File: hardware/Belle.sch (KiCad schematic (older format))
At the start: 18 parts, among them P1 Bell CONN, P2 Battery CONN, P3 Flashing CONN, U1 74AHC1G14, U2 ESP-12, U3 AP2112

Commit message: interchange bell connectors #6
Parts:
- R2: value 51k -> 47k
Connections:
- net +3V3: now also P1.1 (P1); no longer R1.1
- net GND: now also R1.1; no longer P1.1 (P1)
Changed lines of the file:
@@
 P 2800 3500
 F 0 "R2" V 2900 3450 50  0000 L CNN
-F 1 "51k" V 2700 3450 50  0000 L CNN
+F 1 "47k" V 2700 3450 50  0000 L CNN
 F 2 "Resistors_SMD:R_1206_HandSoldering" H 2800 3500 50  0001 C CNN
 F 3 "" H 2800 3500 50  0000 C CNN
@@
 L +3.3V #PWR07
 U 1 1 58BBD349
-P 2400 3100
-F 0 "#PWR07" H 2400 2950 50  0001 C CNN
-F 1 "+3.3V" H 2400 3240 50  0000 C CNN
-F 2 "" H 2400 3100 50  0000 C CNN
-F 3 "" H 2400 3100 50  0000 C CNN
-	1    2400 3100
+P 2550 3900
+F 0 "#PWR07" H 2550 3750 50  0001 C CNN
+F 1 "+3.3V" H 2550 4040 50  0000 C CNN
+F 2 "" H 2550 3900 50  0000 C CNN
+F 3 "" H 2550 3900 50  0000 C CNN
+	1    2550 3900
 	1    0    0    -1
 $EndComp
@@
 L GND #PWR08
 U 1 1 58BBD44E
-P 2400 3750
-F 0 "#PWR08" H 2400 3500 50  0001 C CNN
-F 1 "GND" H 2400 3600 50  0000 C CNN
-F 2 "" H 2400 3750 50  0000 C CNN
-F 3 "" H 2400 3750 50  0000 C CNN
-	1    2400 3750
+P 2600 3050
+F 0 "#PWR08" H 2600 2800 50  0001 C CNN
+F 1 "GND" H 2600 2900 50  0000 C CNN
+F 2 "" H 2600 3050 50  0000 C CNN
+F 3 "" H 2600 3050 50  0000 C CNN
+	1    2600 3050
 	1    0    0    -1
 $EndComp
@@
 	2350 3500 2700 3500
 Wire Wire Line
-	2400 3600 2400 3750
-Wire Wire Line
 	4800 3700 5000 3700
 Wire Wire Line
@@
 Wire Wire Line
 	2400 3600 2350 3600
-Wire Wire Line
-	2400 3400 2400 3500
 Connection ~ 2400 3500
 Wire Wire Line
-	2400 3100 2400 3200
+	2400 3200 2400 3050
+Wire Wire Line
+	2400 3050 2600 3050
+Wire Wire Line
+	2400 3500 2400 3400
+Wire Wire Line
+	2400 3600 2400 3900
+Wire Wire Line
+	2400 3900 2550 3900
 $EndSCHEMATC

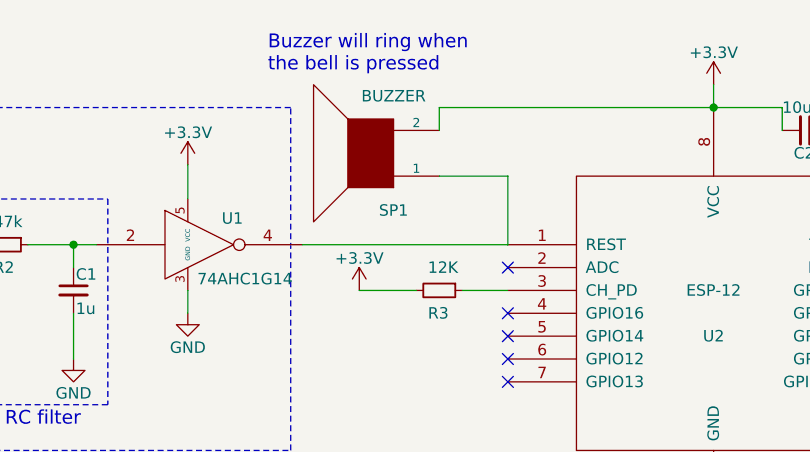
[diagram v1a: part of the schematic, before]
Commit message: add 10k resistor between RESET and Smidth Trigger output
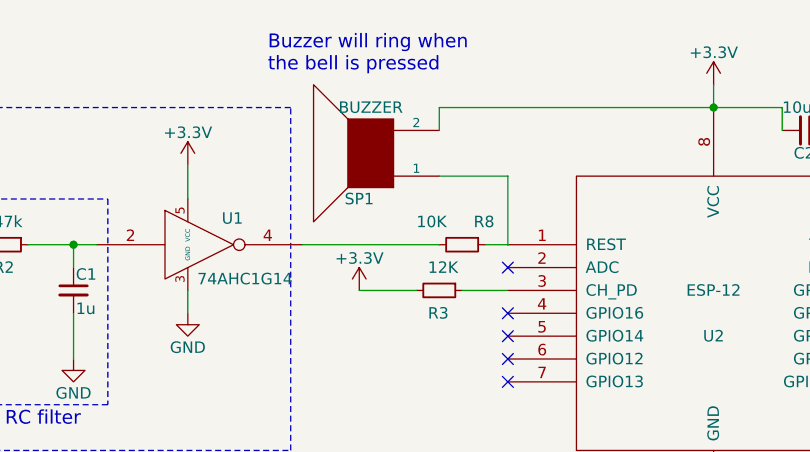
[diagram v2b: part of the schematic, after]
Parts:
- added R8: 10K, symbol R_Small
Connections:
- net at SP1.1, U2.1 (REST): now also R8.1; no longer U1.4
- new net: R8.2, U1.4
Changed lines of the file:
@@
 $EndComp
 $Comp
-L GND #PWR01
+L GND #PWR8
 U 1 1 58BBCCFC
 P 5900 4700
-F 0 "#PWR01" H 5900 4450 50  0001 C CNN
+F 0 "#PWR8" H 5900 4450 50  0001 C CNN
 F 1 "GND" H 5900 4550 50  0000 C CNN
 F 2 "" H 5900 4700 50  0000 C CNN
@@
 $EndComp
 $Comp
-L +3.3V #PWR02
+L +3.3V #PWR7
 U 1 1 58BBCD12
 P 5900 2800
-F 0 "#PWR02" H 5900 2650 50  0001 C CNN
+F 0 "#PWR7" H 5900 2650 50  0001 C CNN
 F 1 "+3.3V" H 5900 2940 50  0000 C CNN
 F 2 "" H 5900 2800 50  0000 C CNN
@@
 $EndComp
 $Comp
-L GND #PWR03
+L GND #PWR9
 U 1 1 58BBCDC5
 P 6650 3000
-F 0 "#PWR03" H 6650 2750 50  0001 C CNN
+F 0 "#PWR9" H 6650 2750 50  0001 C CNN
 F 1 "GND" H 6650 2850 50  0000 C CNN
 F 2 "" H 6650 3000 50  0000 C CNN
@@
 U 1 1 58BBCE20
 P 4400 3100
-F 0 "SP1" H 4300 3350 50  0000 C CNN
-F 1 "BUZZER" H 4300 2850 50  0000 C CNN
+F 0 "SP1" H 4450 3300 50  0000 C CNN
+F 1 "BUZZER" H 4400 2900 50  0000 C CNN
 F 2 "Belle:prosignal_buzzer" H 4400 3100 50  0001 C CNN
 F 3 "" H 4400 3100 50  0000 C CNN
@@
 $EndComp
 $Comp
-L GND #PWR04
+L GND #PWR5
 U 1 1 58BBD0DA
 P 3600 3800
-F 0 "#PWR04" H 3600 3550 50  0001 C CNN
+F 0 "#PWR5" H 3600 3550 50  0001 C CNN
 F 1 "GND" H 3600 3650 50  0000 C CNN
 F 2 "" H 3600 3800 50  0000 C CNN
@@
 $EndComp
 $Comp
-L +3.3V #PWR05
+L +3.3V #PWR4
 U 1 1 58BBD0F6
 P 3600 3150
-F 0 "#PWR05" H 3600 3000 50  0001 C CNN
+F 0 "#PWR4" H 3600 3000 50  0001 C CNN
 F 1 "+3.3V" H 3600 3290 50  0000 C CNN
 F 2 "" H 3600 3150 50  0000 C CNN
@@
 $EndComp
 $Comp
-L GND #PWR06
+L GND #PWR3
 U 1 1 58BBD1A3
 P 3100 4000
-F 0 "#PWR06" H 3100 3750 50  0001 C CNN
+F 0 "#PWR3" H 3100 3750 50  0001 C CNN
 F 1 "GND" H 3100 3850 50  0000 C CNN
 F 2 "" H 3100 4000 50  0000 C CNN
@@
 $EndComp
 $Comp
-L +3.3V #PWR07
+L +3.3V #PWR1
 U 1 1 58BBD349
 P 2550 3900
-F 0 "#PWR07" H 2550 3750 50  0001 C CNN
+F 0 "#PWR1" H 2550 3750 50  0001 C CNN
 F 1 "+3.3V" H 2550 4040 50  0000 C CNN
 F 2 "" H 2550 3900 50  0000 C CNN
@@
 $EndComp
 $Comp
-L GND #PWR08
+L GND #PWR2
 U 1 1 58BBD44E
 P 2600 3050
-F 0 "#PWR08" H 2600 2800 50  0001 C CNN
+F 0 "#PWR2" H 2600 2800 50  0001 C CNN
 F 1 "GND" H 2600 2900 50  0000 C CNN
 F 2 "" H 2600 3050 50  0000 C CNN
@@
 $EndComp
 $Comp
-L +3.3V #PWR09
+L +3.3V #PWR6
 U 1 1 58BBD4B2
 P 4350 3700
-F 0 "#PWR09" H 4350 3550 50  0001 C CNN
+F 0 "#PWR6" H 4350 3550 50  0001 C CNN
 F 1 "+3.3V" H 4350 3840 50  0000 C CNN
 F 2 "" H 4350 3700 50  0000 C CNN
@@
 $EndComp
 $Comp
-L +3.3V #PWR010
+L +3.3V #PWR14
 U 1 1 58BBD5B6
 P 7450 3900
-F 0 "#PWR010" H 7450 3750 50  0001 C CNN
+F 0 "#PWR14" H 7450 3750 50  0001 C CNN
 F 1 "+3.3V" H 7450 4040 50  0000 C CNN
 F 2 "" H 7450 3900 50  0000 C CNN
@@
 $EndComp
 $Comp
-L GND #PWR011
+L GND #PWR10
 U 1 1 58BBD6CB
 P 6800 4400
-F 0 "#PWR011" H 6800 4150 50  0001 C CNN
+F 0 "#PWR10" H 6800 4150 50  0001 C CNN
 F 1 "GND" H 6800 4250 50  0000 C CNN
 F 2 "" H 6800 4400 50  0000 C CNN
@@
 $EndComp
 $Comp
-L +3.3V #PWR012
+L +3.3V #PWR13
 U 1 1 58BBDA6C
 P 7150 4450
-F 0 "#PWR012" H 7150 4300 50  0001 C CNN
+F 0 "#PWR13" H 7150 4300 50  0001 C CNN
 F 1 "+3.3V" H 7150 4590 50  0000 C CNN
 F 2 "" H 7150 4450 50  0000 C CNN
@@
 $EndComp
 $Comp
-L GND #PWR013
+L GND #PWR15
 U 1 1 58BBDB81
 P 7600 5250
-F 0 "#PWR013" H 7600 5000 50  0001 C CNN
+F 0 "#PWR15" H 7600 5000 50  0001 C CNN
 F 1 "GND" H 7600 5100 50  0000 C CNN
 F 2 "" H 7600 5250 50  0000 C CNN
@@
 $EndComp
 $Comp
-L GND #PWR014
+L GND #PWR17
 U 1 1 58BBDD34
 P 8400 5150
-F 0 "#PWR014" H 8400 4900 50  0001 C CNN
+F 0 "#PWR17" H 8400 4900 50  0001 C CNN
 F 1 "GND" H 8400 5000 50  0000 C CNN
 F 2 "" H 8400 5150 50  0000 C CNN
@@
 $EndComp
 $Comp
-L GND #PWR015
+L GND #PWR16
 U 1 1 58BBDF88
 P 8200 4000
-F 0 "#PWR015" H 8200 3750 50  0001 C CNN
+F 0 "#PWR16" H 8200 3750 50  0001 C CNN
 F 1 "GND" H 8200 3850 50  0000 C CNN
 F 2 "" H 8200 4000 50  0000 C CNN
@@
 $EndComp
 $Comp
-L +3.3V #PWR016
+L +3.3V #PWR12
 U 1 1 58BBED05
 P 7150 2700
-F 0 "#PWR016" H 7150 2550 50  0001 C CNN
+F 0 "#PWR12" H 7150 2550 50  0001 C CNN
 F 1 "+3.3V" H 7150 2840 50  0000 C CNN
 F 2 "" H 7150 2700 50  0000 C CNN
@@
 NoConn ~ 6800 3800
 $Comp
-L PWR_FLAG #FLG017
+L PWR_FLAG #FLG1
 U 1 1 58BBEBAB
 P 8200 4850
-F 0 "#FLG017" H 8200 4945 50  0001 C CNN
+F 0 "#FLG1" H 8200 4945 50  0001 C CNN
 F 1 "PWR_FLAG" H 8250 5050 50  0000 C CNN
 F 2 "" H 8200 4850 50  0000 C CNN
@@
 $EndComp
 $Comp
-L GND #PWR018
+L GND #PWR18
 U 1 1 58CE4ED3
 P 8500 4300
-F 0 "#PWR018" H 8500 4050 50  0001 C CNN
+F 0 "#PWR18" H 8500 4050 50  0001 C CNN
 F 1 "GND" H 8500 4150 50  0000 C CNN
 F 2 "" H 8500 4300 50  0000 C CNN
@@
 $EndComp
 $Comp
-L GND #PWR019
+L GND #PWR11
 U 1 1 58CE504A
 P 6800 5000
-F 0 "#PWR019" H 6800 4750 50  0001 C CNN
+F 0 "#PWR11" H 6800 4750 50  0001 C CNN
 F 1 "GND" H 6800 4850 50  0000 C CNN
 F 2 "" H 6800 5000 50  0000 C CNN
@@
 	3600 3700 3600 3800
 Wire Wire Line
-	5000 3500 4100 3500
-Wire Wire Line
 	2900 3500 3200 3500
 Wire Wire Line
@@
 Wire Wire Line
 	2400 3900 2550 3900
+$Comp
+L R_Small R8
+U 1 1 58FE989D
+P 4800 3500
+F 0 "R8" V 4700 3550 50  0000 L CNN
+F 1 "10K" V 4700 3300 50  0000 L CNN
+F 2 "" H 4800 3500 50  0000 C CNN
+F 3 "" H 4800 3500 50  0000 C CNN
+	1    4800 3500
+	0    1    1    0
+$EndComp
+Wire Wire Line
+	5000 3500 4900 3500
+Wire Wire Line
+	4700 3500 4100 3500
 $EndSCHEMATC

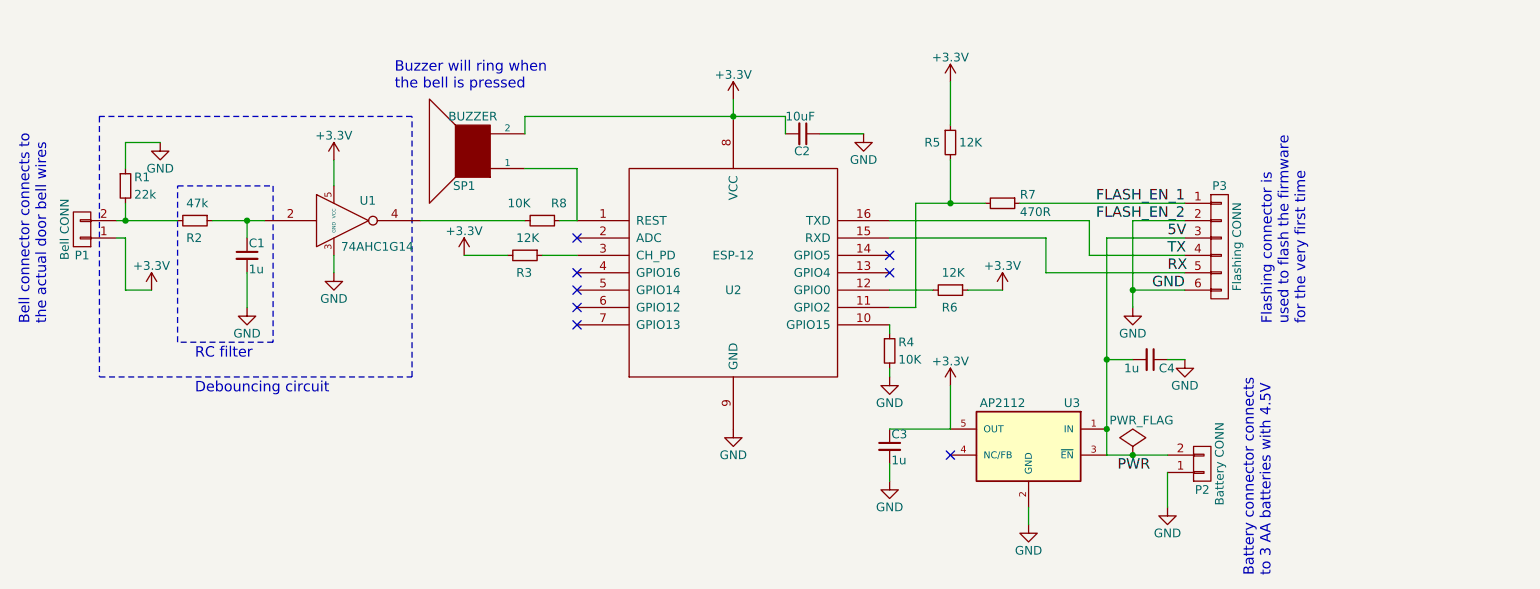
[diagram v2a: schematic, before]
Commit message: add extra capacitors. close #3
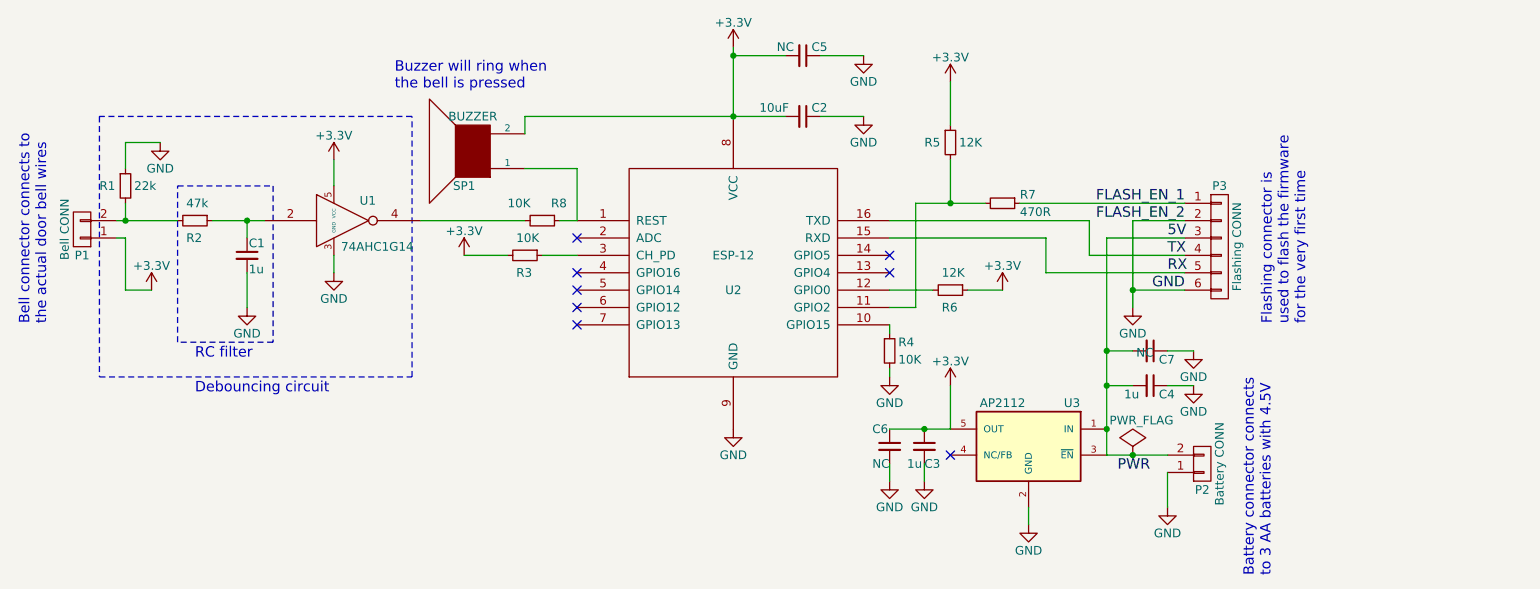
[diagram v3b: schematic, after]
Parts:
- added C5, C6, C7: NC, symbol C_Small
- R3: value 12K -> 10K
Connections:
- net +3V3: now also C5.2, C6.1
- net 5V: now also C7.2
- net GND: now also C5.1, C6.2, C7.1
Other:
- moved on the sheet: C2, C3, C4

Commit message: arrange flashing connector as default FTDI pin. close #5
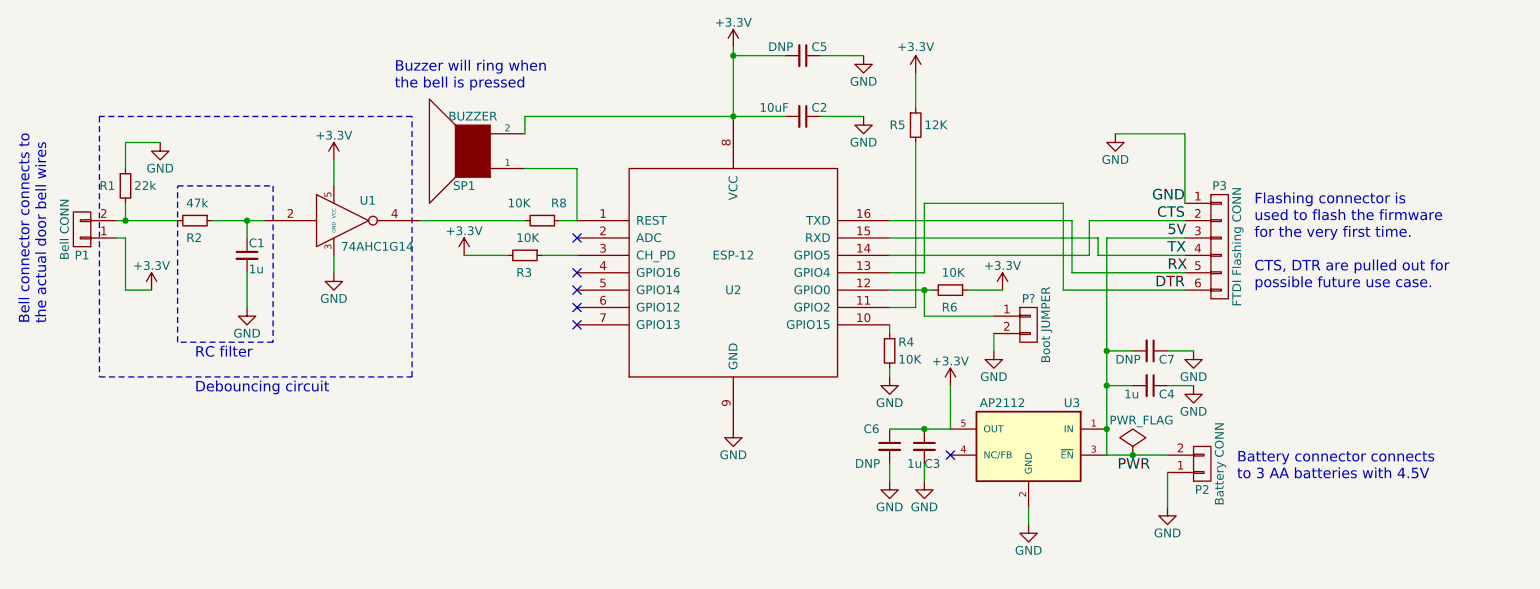
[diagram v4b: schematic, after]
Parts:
- removed R7: 470R, Resistors_SMD:R_1206_HandSoldering, symbol R_Small
- added P?: Boot JUMPER, symbol CONN_01X02
- C5, C6, C7: value NC -> DNP
- P3: value Flashing CONN -> FTDI Flashing CONN
- R6: value 12K -> 10K
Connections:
- net FLASH_EN_1 is gone; now on net GND: P3.1 (P1)
- net GND: now also P?.2 (P2); no longer P3.2 (P2), P3.6 (P6)
- net RX: now also U2.16 (TXD); no longer U2.15 (RXD)
- net TX: now also U2.15 (RXD); no longer U2.16 (TXD)
- net at R6.2, U2.12 (GPIO0): now also P?.1 (P1)
- net DTR: now reaches U2.13 (GPIO4)
- net DTR: now also P3.6 (P6)
- net CTS: now reaches U2.14 (GPIO5)
- net CTS: now also P3.2 (P2)
- no-connect marks 8 -> 6
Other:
- note added: "Flashing connector is\nused to flash the firmware\nfor the very first time.\n\nCTS, DTR are pulled out for\npossible future use case."
- note removed: "Flashing connector is\nused to flash the firmware\nfor the very first time"
- moved on the sheet: R5
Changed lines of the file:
@@
 P 7150 3900
 F 0 "R6" V 7250 3850 50  0000 L CNN
-F 1 "12K" V 7050 3850 50  0000 L CNN
+F 1 "10K" V 7050 3850 50  0000 L CNN
 F 2 "Resistors_SMD:R_1206_HandSoldering" H 7150 3900 50  0001 C CNN
 F 3 "" H 7150 3900 50  0000 C CNN
@@
 P 8700 3650
 F 0 "P3" H 8700 4000 50  0000 C CNN
-F 1 "Flashing CONN" V 8800 3650 50  0000 C CNN
+F 1 "FTDI Flashing CONN" V 8800 3650 50  0000 C CNN
 F 2 "Pin_Headers:Pin_Header_Straight_1x06_Pitch2.54mm" H 8700 3650 50  0001 C CNN
 F 3 "" H 8700 3650 50  0000 C CNN
@@
 L GND #PWR015
 U 1 1 58BBDF88
-P 8200 4000
-F 0 "#PWR015" H 8200 3750 50  0001 C CNN
-F 1 "GND" H 8200 3850 50  0000 C CNN
-F 2 "" H 8200 4000 50  0000 C CNN
-F 3 "" H 8200 4000 50  0000 C CNN
-	1    8200 4000
+P 8100 3000
+F 0 "#PWR015" H 8100 2750 50  0001 C CNN
+F 1 "GND" H 8100 2850 50  0000 C CNN
+F 2 "" H 8100 3000 50  0000 C CNN
+F 3 "" H 8100 3000 50  0000 C CNN
+	1    8100 3000
 	1    0    0    -1
 $EndComp
@@
 RX
 $Comp
-L R_Small R7
-U 1 1 58BBEBD8
-P 7450 3400
-F 0 "R7" V 7400 3500 50  0000 L CNN
-F 1 "470R" V 7500 3500 50  0000 L CNN
-F 2 "Resistors_SMD:R_1206_HandSoldering" H 7450 3400 50  0001 C CNN
-F 3 "" H 7450 3400 50  0000 C CNN
-	1    7450 3400
-	0    1    1    0
-$EndComp
-$Comp
 L R_Small R5
 U 1 1 58BBEC6E
-P 7150 3050
-F 0 "R5" H 7000 3050 50  0000 L CNN
-F 1 "12K" H 7200 3050 50  0000 L CNN
-F 2 "Resistors_SMD:R_1206_HandSoldering" H 7150 3050 50  0001 C CNN
-F 3 "" H 7150 3050 50  0000 C CNN
-	1    7150 3050
+P 6950 2950
+F 0 "R5" H 6800 2950 50  0000 L CNN
+F 1 "12K" H 7000 2950 50  0000 L CNN
+F 2 "Resistors_SMD:R_1206_HandSoldering" H 6950 2950 50  0001 C CNN
+F 3 "" H 6950 2950 50  0000 C CNN
+	1    6950 2950
 	1    0    0    -1
 $EndComp
@@
 L +3.3V #PWR016
 U 1 1 58BBED05
-P 7150 2700
-F 0 "#PWR016" H 7150 2550 50  0001 C CNN
-F 1 "+3.3V" H 7150 2840 50  0000 C CNN
-F 2 "" H 7150 2700 50  0000 C CNN
-F 3 "" H 7150 2700 50  0000 C CNN
-	1    7150 2700
+P 6950 2650
+F 0 "#PWR016" H 6950 2500 50  0001 C CNN
+F 1 "+3.3V" H 6950 2800 50  0000 C CNN
+F 2 "" H 6950 2650 50  0000 C CNN
+F 3 "" H 6950 2650 50  0000 C CNN
+	1    6950 2650
 	1    0    0    -1
 $EndComp
@@
 5V
 Text Label 8500 3500 2    60   ~ 0
-FLASH_EN_2
+CTS
 Text Label 8500 3400 2    60   ~ 0
-FLASH_EN_1
+GND
 Text Label 8500 3900 2    60   ~ 0
-GND
+DTR
 Text Label 8300 4950 2    60   ~ 0
 PWR
@@
 NoConn ~ 5000 3600
 NoConn ~ 7150 4850
-NoConn ~ 6800 3700
-NoConn ~ 6800 3800
 $Comp
 L PWR_FLAG #FLG017
@@
 Text Notes 3950 2750 0    60   ~ 0
 Buzzer will ring when \nthe bell is pressed
-Text Notes 9200 4100 1    60   ~ 0
-Flashing connector is\nused to flash the firmware\nfor the very first time
+Text Notes 8900 3900 0    60   ~ 0
+Flashing connector is\nused to flash the firmware\nfor the very first time.\n\nCTS, DTR are pulled out for\npossible future use case.
 Text Notes 1950 4100 1    60   ~ 0
 Bell connector connects to \nthe actual door bell wires
-Text Notes 9000 5550 1    60   ~ 0
+Text Notes 8800 5000 0    60   ~ 0
 Battery connector connects \nto 3 AA batteries with 4.5V
 Text Notes 2800 4300 0    60   ~ 0
@@
 	3600 3700 3600 3800
 Wire Wire Line
-	2900 3500 3200 3500
+	2900 3500 3100 3500
+Wire Wire Line
+	3100 3500 3200 3500
 Wire Wire Line
 	3100 3600 3100 3500
@@
 	3100 3800 3100 4000
 Wire Wire Line
-	2350 3500 2700 3500
+	2350 3500 2400 3500
+Wire Wire Line
+	2400 3500 2700 3500
 Wire Wire Line
 	4800 3700 5000 3700
@@
 	4600 3700 4350 3700
 Wire Wire Line
-	6800 3900 7050 3900
+	6800 3900 7000 3900
+Wire Wire Line
+	7000 3900 7050 3900
 Wire Wire Line
 	7250 3900 7450 3900
@@
 	7600 5150 7600 5250
 Wire Wire Line
-	8050 4850 8400 4850
-Wire Wire Line
-	8050 3600 8050 4850
+	8050 4850 8200 4850
+Wire Wire Line
+	8200 4850 8400 4850
+Wire Wire Line
+	8050 3600 8050 4250
+Wire Wire Line
+	8050 4250 8050 4450
+Wire Wire Line
+	8050 4450 8050 4700
+Wire Wire Line
+	8050 4700 8050 4850
 Wire Wire Line
 	8400 4950 8400 5150
-Wire Wire Line
-	7700 3800 7700 3600
-Wire Wire Line
-	7700 3600 6800 3600
-Wire Wire Line
-	8500 3700 7950 3700
-Wire Wire Line
-	7950 3700 7950 3500
-Wire Wire Line
-	7950 3500 6800 3500
 Wire Wire Line
 	8500 3600 8050 3600
 Connection ~ 8050 4700
 Wire Wire Line
-	8500 3500 8200 3500
-Wire Wire Line
-	8200 3500 8200 4000
-Connection ~ 8200 3900
-Wire Wire Line
 	6800 4000 6950 4000
-Wire Wire Line
-	6950 4000 6950 3400
-Wire Wire Line
-	6950 3400 7350 3400
-Wire Wire Line
-	7550 3400 8500 3400
-Wire Wire Line
-	7150 2700 7150 2950
-Wire Wire Line
-	7150 3150 7150 3400
-Connection ~ 7150 3400
 Connection ~ 8200 4850
 Wire Wire Line
@@
 	4700 3500 4100 3500
 Wire Wire Line
-	4700 2900 6200 2900
+	4700 2900 5900 2900
+Wire Wire Line
+	5900 2900 6200 2900
 $Comp
 L C_Small C5
@@
 P 6300 2550
 F 0 "C5" V 6250 2600 50  0000 L CNN
-F 1 "NC" V 6250 2400 50  0000 L CNN
+F 1 "DNP" V 6250 2350 50  0000 L CNN
 F 2 "" H 6300 2550 50  0000 C CNN
 F 3 "" H 6300 2550 50  0000 C CNN
@@
 $EndComp
 Wire Wire Line
-	5900 2500 5900 2900
+	5900 2500 5900 2550
+Wire Wire Line
+	5900 2550 5900 2900
 Wire Wire Line
 	6200 2550 5900 2550
@@
 P 8300 4250
 F 0 "C7" V 8350 4300 50  0000 L CNN
-F 1 "NC" V 8310 4170 50  0000 L CNN
+F 1 "DNP" V 8350 4050 50  0000 L CNN
 F 2 "" H 8300 4250 50  0000 C CNN
 F 3 "" H 8300 4250 50  0000 C CNN
@@
 U 1 1 590712F7
 P 6800 4800
-F 0 "C6" H 6700 4900 50  0000 L CNN
-F 1 "NC" H 6700 4700 50  0000 L CNN
+F 0 "C6" H 6650 4900 50  0000 L CNN
+F 1 "DNP" H 6600 4700 50  0000 L CNN
 F 2 "" H 6800 4800 50  0000 C CNN
 F 3 "" H 6800 4800 50  0000 C CNN
@@
 	7000 4900 7000 5000
 Wire Wire Line
-	8500 3800 7700 3800
-Wire Wire Line
-	8500 3900 8200 3900
-Wire Wire Line
-	6800 4700 7150 4700
+	6800 4700 7000 4700
+Wire Wire Line
+	7000 4700 7150 4700
 Connection ~ 7000 4700
+Wire Wire Line
+	6950 4000 6950 3050
+Wire Wire Line
+	6950 2850 6950 2650
+Wire Wire Line
+	6800 3500 7850 3500
+Wire Wire Line
+	7850 3500 7850 3800
+Wire Wire Line
+	7850 3800 8500 3800
+Wire Wire Line
+	6800 3600 8000 3600
+Wire Wire Line
+	8000 3600 8000 3700
+Wire Wire Line
+	8000 3700 8500 3700
+Wire Wire Line
+	8500 3400 8500 3000
+Wire Wire Line
+	8500 3000 8100 3000
+$Comp
+L CONN_01X02 P?
+U 1 1 59074415
+P 7600 4100
+F 0 "P?" H 7600 4250 50  0000 C CNN
+F 1 "Boot JUMPER" V 7700 4100 50  0000 C CNN
+F 2 "" H 7600 4100 50  0000 C CNN
+F 3 "" H 7600 4100 50  0000 C CNN
+	1    7600 4100
+	1    0    0    -1
+$EndComp
+Wire Wire Line
+	7000 3900 7000 4050
+Wire Wire Line
+	7000 4050 7400 4050
+Connection ~ 7000 3900
+$Comp
+L GND #PWR?
+U 1 1 59074532
+P 7400 4250
+F 0 "#PWR?" H 7400 4000 50  0001 C CNN
+F 1 "GND" H 7400 4100 50  0000 C CNN
+F 2 "" H 7400 4250 50  0000 C CNN
+F 3 "" H 7400 4250 50  0000 C CNN
+	1    7400 4250
+	1    0    0    -1
+$EndComp
+Wire Wire Line
+	7400 4150 7400 4250
+Wire Wire Line
+	6800 3700 7950 3700
+Wire Wire Line
+	7950 3700 7950 3500
+Wire Wire Line
+	7950 3500 8300 3500
+Wire Wire Line
+	8300 3500 8300 3500
+Wire Wire Line
+	8300 3500 8500 3500
+Wire Wire Line
+	6800 3800 7000 3800
+Wire Wire Line
+	7000 3800 7000 3400
+Wire Wire Line
+	7000 3400 7800 3400
+Wire Wire Line
+	7800 3400 7800 3900
+Wire Wire Line
+	7800 3900 8500 3900
 $EndSCHEMATC
